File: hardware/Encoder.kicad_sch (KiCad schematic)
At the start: 8 parts, among them SW1 N/A

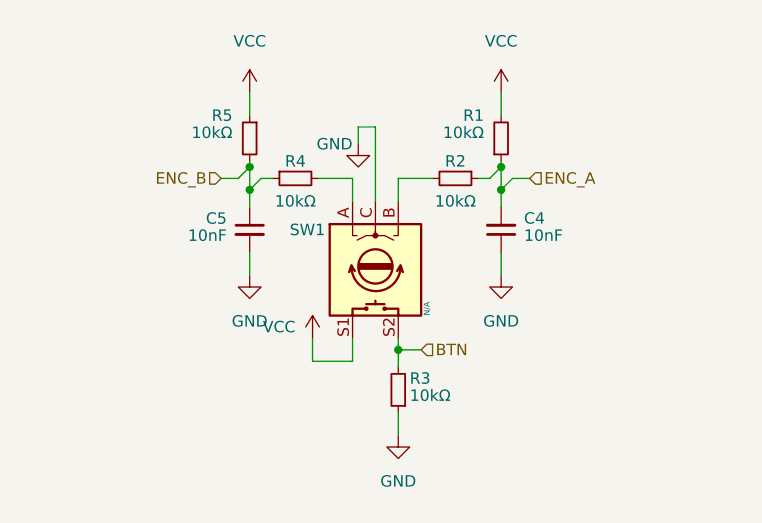
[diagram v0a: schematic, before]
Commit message: v2 Board Ready - Added Art - Removed DRC/ERC - Finished BOM
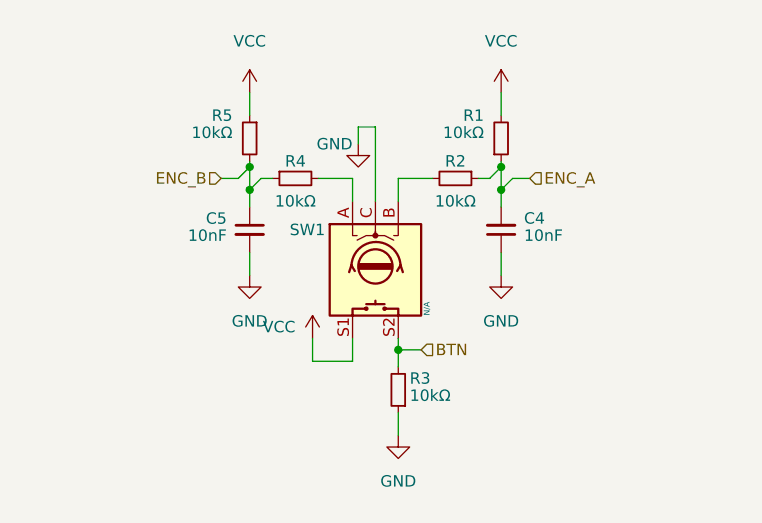
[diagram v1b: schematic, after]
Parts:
- C4, C5: Comments (none) -> Any X7R, 0603, 10V cap.; Digikey PN (none) -> 1276-1009-1-ND; Farnell PN (none) -> 3013408; MPN (none) -> CL10B103KB8NNNC; Manufacturer (none) -> Samsung; Tolerance (none) -> X7R; Vrating (none) -> 50V
- R1, R2, R3, R4, R5: Comments (none) -> Any 10kΩ. Why are you buying these? You should have some so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; Digikey PN (none) -> 311-10KARCT-ND; Farnell PN (none) -> 2073612; MPN (none) -> RC0805JR-0710KL; Manufacturer (none) -> Yageo

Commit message: Getting ready for KiBot. Removed some old references to 3D models from some parts
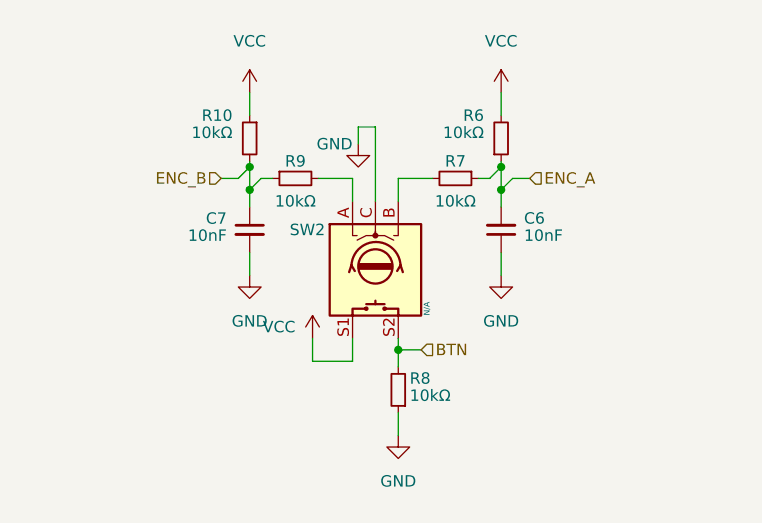
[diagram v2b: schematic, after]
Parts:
- renumbered C4 to C6, C5 to C7, R5 to R10, R1 to R6, R2 to R7, R3 to R8, R4 to R9, SW1 to SW2
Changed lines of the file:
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@@
   (symbol (lib_id "Device:R_Small") (at 67.945 47.625 270) (unit 1)
     (in_bom yes) (on_board yes) (dnp no)
-    (property "Reference" "R2" (at 67.945 45.72 90)
+    (property "Reference" "R7" (at 67.945 45.72 90)
       (effects (font (size 1.27 1.27)))
     )
@@
   (symbol (lib_id "Device:R_Small") (at 73.025 43.18 0) (mirror x) (unit 1)
     (in_bom yes) (on_board yes) (dnp no)
-    (property "Reference" "R1" (at 71.12 40.64 0)
+    (property "Reference" "R6" (at 71.12 40.64 0)
       (effects (font (size 1.27 1.27)) (justify right))
     )
@@
   (symbol (lib_id "Device:R_Small") (at 61.595 71.12 180) (unit 1)
     (in_bom yes) (on_board yes) (dnp no)
-    (property "Reference" "R3" (at 62.865 69.85 0)
+    (property "Reference" "R8" (at 62.865 69.85 0)
       (effects (font (size 1.27 1.27)) (justify right))
     )
@@
   (symbol (lib_id "Device:RotaryEncoder_Switch") (at 59.055 57.785 90) (mirror x) (unit 1)
     (in_bom yes) (on_board yes) (dnp no)
-    (property "Reference" "SW1" (at 49.53 53.34 90)
+    (property "Reference" "SW2" (at 49.53 53.34 90)
       (effects (font (size 1.27 1.27)) (justify right))
     )
@@
   (symbol (lib_id "power:GND") (at 45.085 58.42 0) (mirror y) (unit 1)
     (in_bom yes) (on_board yes) (dnp no) (fields_autoplaced)
-    (property "Reference" "#PWR019" (at 45.085 64.77 0)
+    (property "Reference" "#PWR026" (at 45.085 64.77 0)
       (effects (font (size 1.27 1.27)) hide)
     )
@@
   (symbol (lib_id "Device:R_Small") (at 45.085 43.18 0) (mirror y) (unit 1)
     (in_bom yes) (on_board yes) (dnp no)
-    (property "Reference" "R5" (at 43.18 40.64 0)
+    (property "Reference" "R10" (at 43.18 40.64 0)
       (effects (font (size 1.27 1.27)) (justify left))
     )
@@
   (symbol (lib_id "power:VCC") (at 52.07 65.405 0) (mirror y) (unit 1)
     (in_bom yes) (on_board yes) (dnp no) (fields_autoplaced)
-    (property "Reference" "#PWR015" (at 52.07 69.215 0)
+    (property "Reference" "#PWR022" (at 52.07 69.215 0)
       (effects (font (size 1.27 1.27)) hide)
     )
@@
   (symbol (lib_id "power:GND") (at 57.15 43.815 0) (mirror y) (unit 1)
     (in_bom yes) (on_board yes) (dnp no)
-    (property "Reference" "#PWR016" (at 57.15 50.165 0)
+    (property "Reference" "#PWR023" (at 57.15 50.165 0)
       (effects (font (size 1.27 1.27)) hide)
     )
@@
   (symbol (lib_id "power:VCC") (at 45.085 38.1 0) (mirror y) (unit 1)
     (in_bom yes) (on_board yes) (dnp no) (fields_autoplaced)
-    (property "Reference" "#PWR018" (at 45.085 41.91 0)
+    (property "Reference" "#PWR025" (at 45.085 41.91 0)
       (effects (font (size 1.27 1.27)) hide)
     )
@@
   (symbol (lib_id "power:GND") (at 61.595 76.2 0) (unit 1)
     (in_bom yes) (on_board yes) (dnp no) (fields_autoplaced)
-    (property "Reference" "#PWR017" (at 61.595 82.55 0)
+    (property "Reference" "#PWR024" (at 61.595 82.55 0)
       (effects (font (size 1.27 1.27)) hide)
     )
@@
   (symbol (lib_id "Device:C_Small") (at 45.085 53.34 0) (mirror y) (unit 1)
     (in_bom yes) (on_board yes) (dnp no)
-    (property "Reference" "C5" (at 42.545 52.0762 0)
+    (property "Reference" "C7" (at 42.545 52.0762 0)
       (effects (font (size 1.27 1.27)) (justify left))
     )
@@
   (symbol (lib_id "Device:R_Small") (at 50.165 47.625 90) (mirror x) (unit 1)
     (in_bom yes) (on_board yes) (dnp no)
-    (property "Reference" "R4" (at 50.165 45.72 90)
+    (property "Reference" "R9" (at 50.165 45.72 90)
       (effects (font (size 1.27 1.27)))
     )
@@
   (symbol (lib_id "power:VCC") (at 73.025 38.1 0) (mirror y) (unit 1)
     (in_bom yes) (on_board yes) (dnp no) (fields_autoplaced)
-    (property "Reference" "#PWR013" (at 73.025 41.91 0)
+    (property "Reference" "#PWR020" (at 73.025 41.91 0)
       (effects (font (size 1.27 1.27)) hide)
     )
@@
   (symbol (lib_id "Device:C_Small") (at 73.025 53.34 180) (unit 1)
     (in_bom yes) (on_board yes) (dnp no)
-    (property "Reference" "C4" (at 75.565 52.0635 0)
+    (property "Reference" "C6" (at 75.565 52.0635 0)
       (effects (font (size 1.27 1.27)) (justify right))
     )
@@
   (symbol (lib_id "power:GND") (at 73.025 58.42 0) (mirror y) (unit 1)
     (in_bom yes) (on_board yes) (dnp no) (fields_autoplaced)
-    (property "Reference" "#PWR014" (at 73.025 64.77 0)
-      (effects (font (size 1.27 1.27)) hide)
-    )
+    (property "Reference" "#PWR021" (at 73.025 64.77 0)
+      (effects (font (size 1.27 1.27)) hide)
+    )

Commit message: Not sure of the complete list of changes, but fixed a bunch of DRC/ERC errors
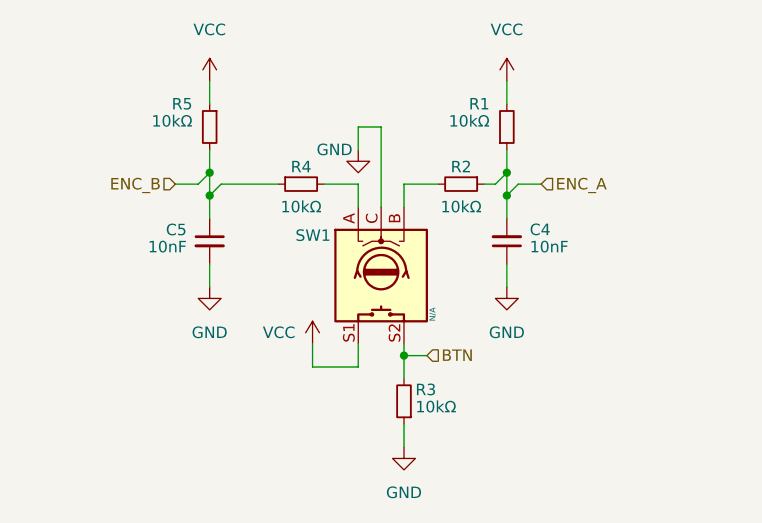
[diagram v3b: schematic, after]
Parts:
- renumbered C6 to C4, C7 to C5, R6 to R1, R7 to R2, R8 to R3, R9 to R4, R10 to R5, SW2 to SW1
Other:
- moved on the sheet: C4, C5, R1, R2, R3, R4, R5, SW1

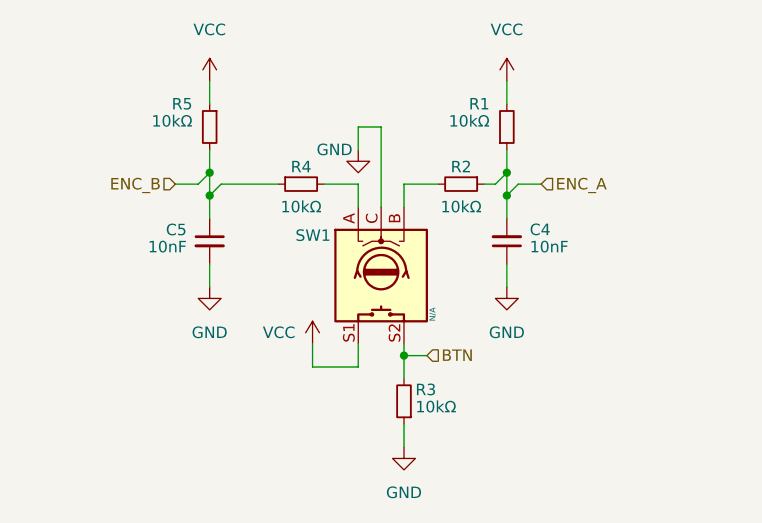
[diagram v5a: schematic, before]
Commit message: Tweaked positions of encoders, smd passive shapes, and rerouted
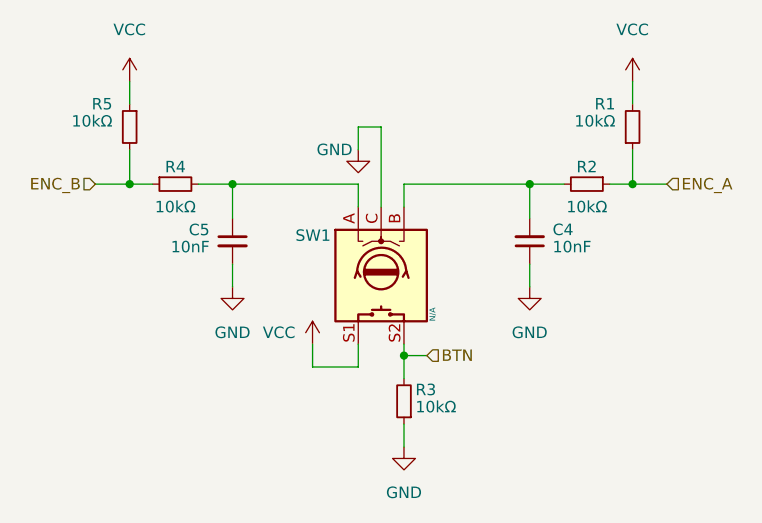
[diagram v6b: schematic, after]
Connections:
- net ENC_A: no longer C4.2
- net ENC_B: no longer C5.1
- net at R2.2, SW1.B: now also C4.2
- net at R4.2, SW1.A: now also C5.1
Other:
- moved on the sheet: C4, C5, R1, R2, R4, R5
